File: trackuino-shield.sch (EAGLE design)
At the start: 26 parts, among them IC2 REG1117, IC3 ON M74VHC1GT125DT1G, IC4 ON M74VHC1GT125DT1G, IC5 ON M74VHC1GT125DT1G, J5 J5MM, J6 J5MM, J7 J5MM, J8 J5MM, M2 HX1, M3 VENUS634FLPX, Q1 PMV20XN, PMV16UN, etc, U1 LM60 int, X1 BU-SMA-V, X2 Vin, X3 LM60 ext, X4 Buzzer

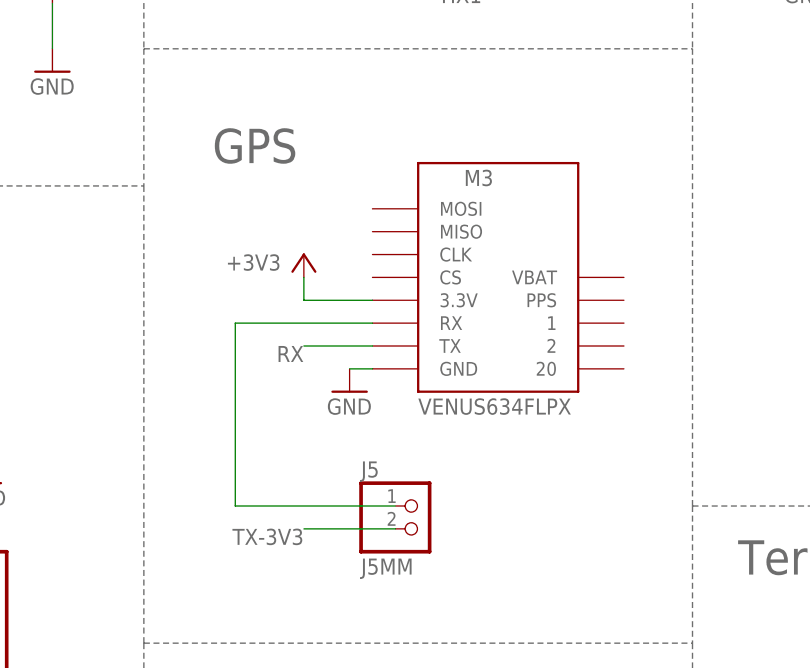
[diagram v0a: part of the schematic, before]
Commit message: Replaced Venus 634FLPx (phased out) with 638FLPx (sparkfun product #11058)
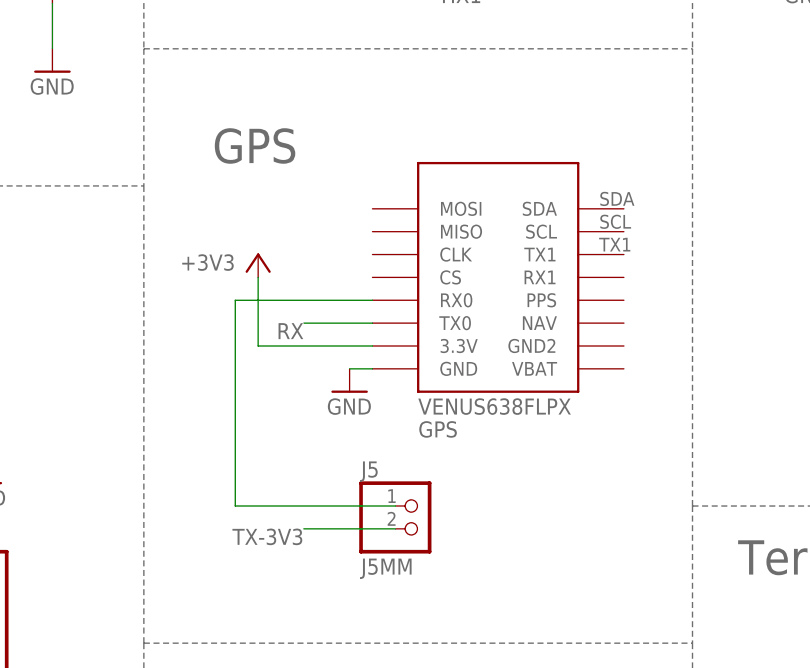
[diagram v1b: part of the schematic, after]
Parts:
- removed M3: VENUS634FLPX, trackuino:VENUS634FLPX
- added GPS: VENUS638FLPX, trackuino:VENUS638FLPX
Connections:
- net +3V3: now also GPS.3.3V; no longer M3.3.3V
- net GND: now also GPS.GND; no longer M3.GND
- net N$2: now also GPS.RX0; no longer M3.RX
- net RX: now also GPS.TX0; no longer M3.TX
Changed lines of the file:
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@@
 <part name="P+1" library="supply1" deviceset="+5V" device=""/>
 <part name="M2" library="trackuino" deviceset="HX1" device=""/>
-<part name="M3" library="trackuino" deviceset="VENUS634FLPX" device=""/>
 <part name="P+3" library="supply1" deviceset="+5V" device=""/>
 <part name="GND7" library="supply1" deviceset="GND" device=""/>
@@
 <part name="R3" library="resistor" deviceset="R-EU_" device="R1206" value="1K"/>
 <part name="IC2" library="burr-brown" deviceset="REG1117" device=""/>
+<part name="GPS" library="trackuino" deviceset="VENUS638FLPX" device=""/>
 </parts>
 <sheets>
@@
 <instance part="P+1" gate="1" x="27.94" y="68.58"/>
 <instance part="M2" gate="G$1" x="101.6" y="147.32" rot="R270"/>
-<instance part="M3" gate="G$1" x="106.68" y="96.52"/>
 <instance part="P+3" gate="1" x="93.98" y="142.24" rot="R90"/>
 <instance part="GND7" gate="1" x="91.44" y="132.08"/>
@@
 <instance part="C2" gate="G$1" x="12.7" y="157.48"/>
 <instance part="+3V3" gate="G$1" x="53.34" y="160.02" rot="R270"/>
-<instance part="+3V1" gate="G$1" x="86.36" y="99.06" smashed="yes">
-<attribute name="VALUE" x="83.82" y="99.06" size="1.778" layer="96" rot="R180"/>
+<instance part="+3V1" gate="G$1" x="81.28" y="99.06" smashed="yes">
+<attribute name="VALUE" x="78.74" y="99.06" size="1.778" layer="96" rot="R180"/>
 </instance>
 <instance part="GND11" gate="1" x="91.44" y="83.82"/>
@@
 <instance part="R3" gate="G$1" x="246.38" y="60.96" rot="R90"/>
 <instance part="IC2" gate="G$1" x="30.48" y="160.02"/>
+<instance part="GPS" gate="G$1" x="106.68" y="93.98"/>
 </instances>
 <busses>
@@
 <segment>
 <wire x1="91.44" y1="86.36" x2="93.98" y2="86.36" width="0.1524" layer="91"/>
-<pinref part="M3" gate="G$1" pin="GND"/>
 <pinref part="GND11" gate="1" pin="GND"/>
+<pinref part="GPS" gate="G$1" pin="GND"/>
 </segment>
 <segment>
@@
 <net name="+3V3" class="2">
 <segment>
-<wire x1="86.36" y1="96.52" x2="86.36" y2="93.98" width="0.1524" layer="91"/>
-<wire x1="86.36" y1="93.98" x2="93.98" y2="93.98" width="0.1524" layer="91"/>
+<wire x1="81.28" y1="96.52" x2="81.28" y2="88.9" width="0.1524" layer="91"/>
+<wire x1="81.28" y1="88.9" x2="93.98" y2="88.9" width="0.1524" layer="91"/>
 <pinref part="+3V1" gate="G$1" pin="+3V3"/>
-<pinref part="M3" gate="G$1" pin="3.3V"/>
+<pinref part="GPS" gate="G$1" pin="3.3V"/>
 </segment>
 <segment>
@@
 </segment>
 <segment>
-<wire x1="93.98" y1="88.9" x2="86.36" y2="88.9" width="0.1524" layer="91"/>
-<label x="86.36" y="88.9" size="1.778" layer="95" rot="R180"/>
-<pinref part="M3" gate="G$1" pin="TX"/>
+<wire x1="93.98" y1="91.44" x2="86.36" y2="91.44" width="0.1524" layer="91"/>
+<label x="86.36" y="91.44" size="1.778" layer="95" rot="R180"/>
+<pinref part="GPS" gate="G$1" pin="TX0"/>
 </segment>
 </net>
@@
 <segment>
 <wire x1="96.52" y1="71.12" x2="78.74" y2="71.12" width="0.1524" layer="91"/>
-<wire x1="78.74" y1="71.12" x2="78.74" y2="91.44" width="0.1524" layer="91"/>
-<wire x1="78.74" y1="91.44" x2="93.98" y2="91.44" width="0.1524" layer="91"/>
+<wire x1="78.74" y1="71.12" x2="78.74" y2="93.98" width="0.1524" layer="91"/>
+<wire x1="78.74" y1="93.98" x2="93.98" y2="93.98" width="0.1524" layer="91"/>
 <pinref part="J5" gate="G$1" pin="1"/>
-<pinref part="M3" gate="G$1" pin="RX"/>
-</segment>
-</net>
+<pinref part="GPS" gate="G$1" pin="RX0"/>
+</segment>
+</net>

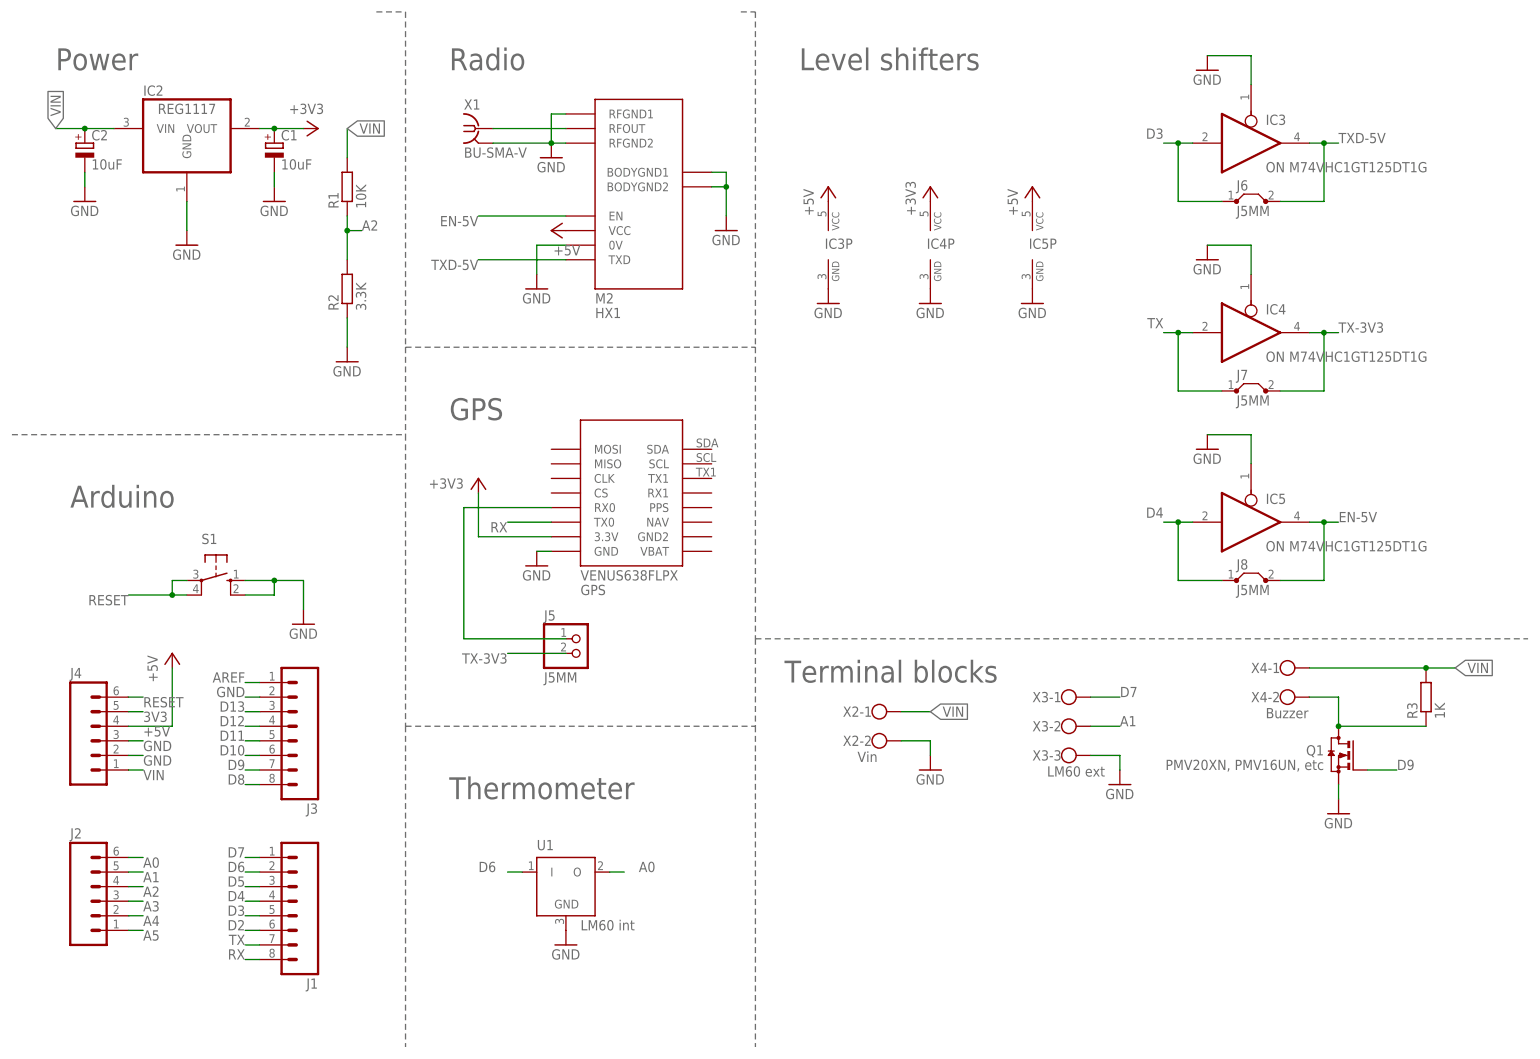
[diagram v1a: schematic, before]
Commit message: Updated footprint of the GPS to the newest breakout board for the (Venus638FLPx)
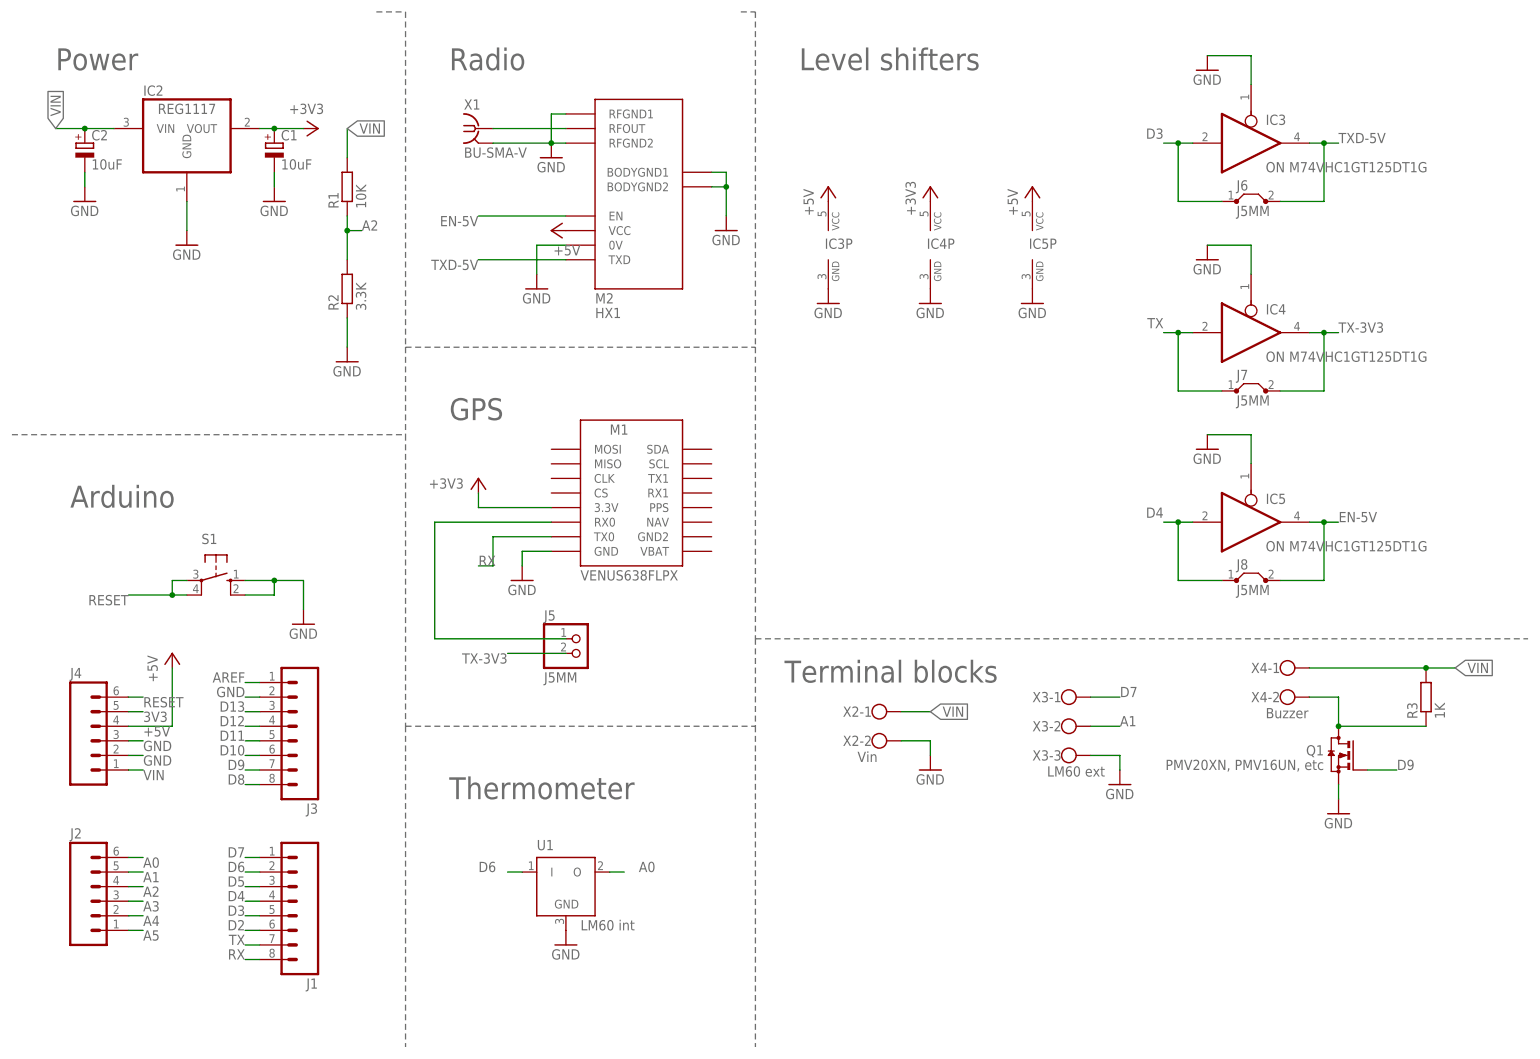
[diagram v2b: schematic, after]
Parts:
- removed GPS: VENUS638FLPX, trackuino:VENUS638FLPX
- added M1: VENUS638FLPX, Venus638FLPx:VENUS638FLPX
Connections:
- net +3V3: now also M1.3.3V; no longer GPS.3.3V
- net GND: now also M1.GND; no longer GPS.GND
- net N$2: now also M1.RX0; no longer GPS.RX0
- net RX: now also M1.TX0; no longer GPS.TX0
